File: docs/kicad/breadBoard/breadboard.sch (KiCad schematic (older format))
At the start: 16 parts

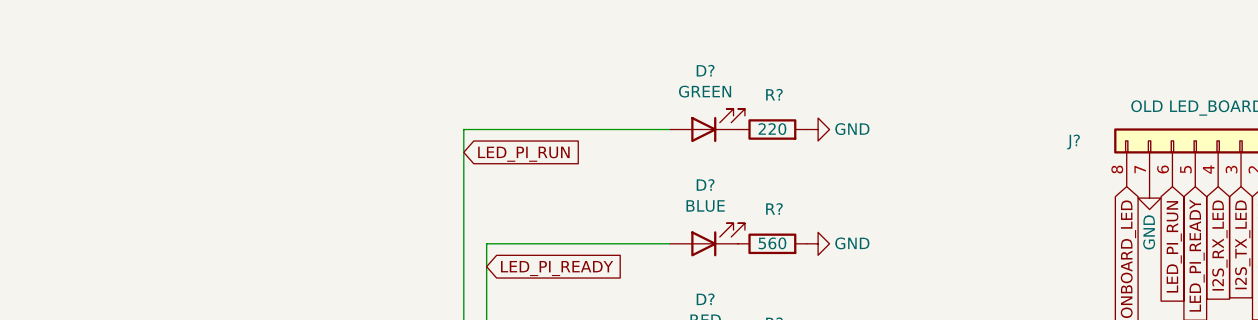
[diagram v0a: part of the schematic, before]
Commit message: add comments to Schematics
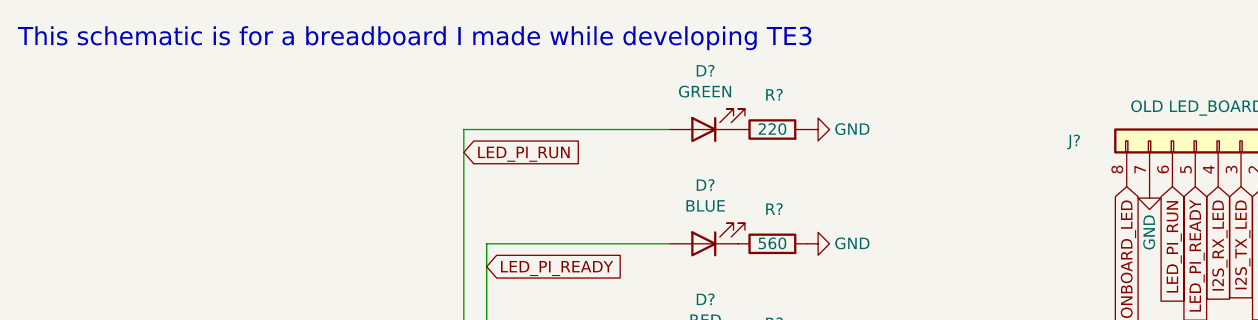
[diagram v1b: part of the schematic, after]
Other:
- note added: "This schematic is for a breadboard I made while developing TE3"
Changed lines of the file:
@@
 	0    -1   -1   0
 $EndComp
+Text Notes 1050 700  0    79   ~ 0
+This schematic is for a breadboard I made while developing TE3
 $EndSCHEMATC
